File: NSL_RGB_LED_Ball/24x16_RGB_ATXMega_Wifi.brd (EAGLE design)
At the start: 46.4 x 123.7 mm, 109 parts, among them IC2 TLC5947XLP, IC3 TLC5947XLP, IC4 TLC5947XLP, IC5 MCP73123, IC6 BLUETOOTH-RN41", IC7 MMA7455L, IC8 OPA344, Q1 BSH201, X1 NX3225GA XC1972CT-ND

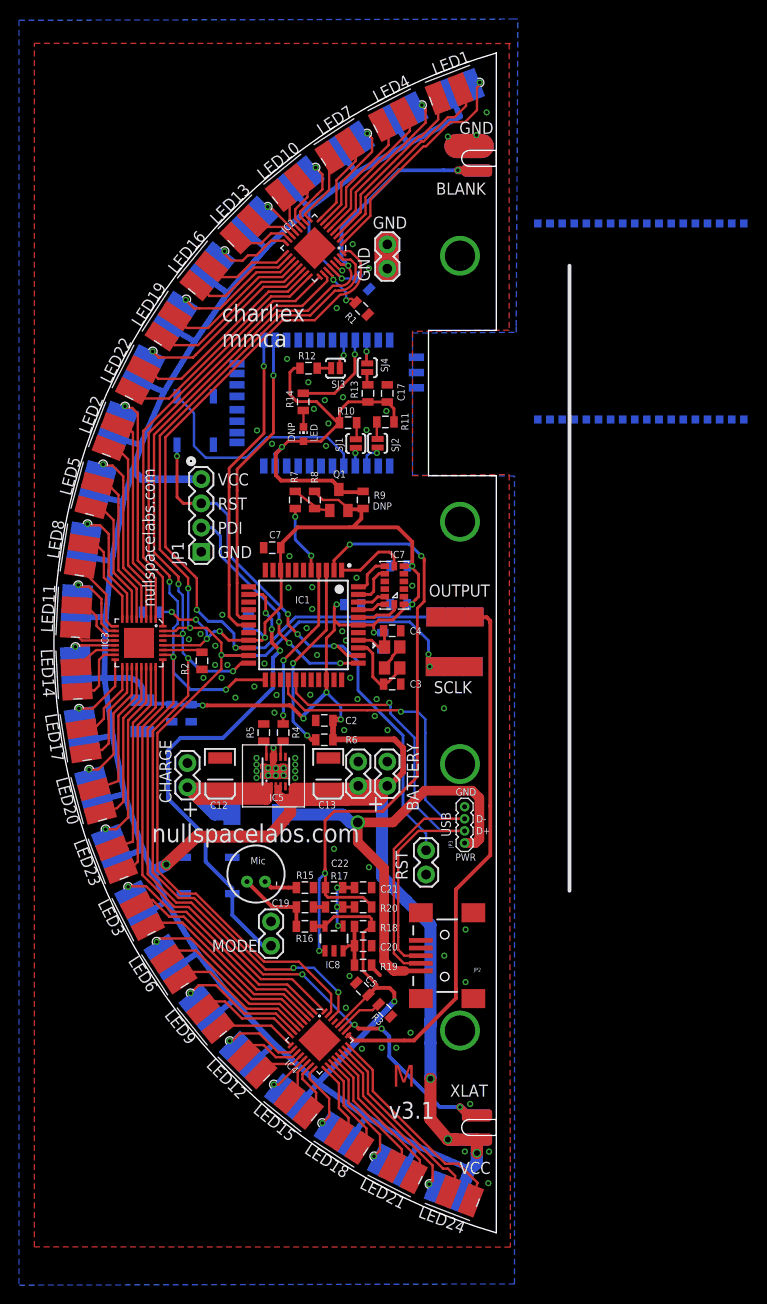
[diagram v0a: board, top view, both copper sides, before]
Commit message: 
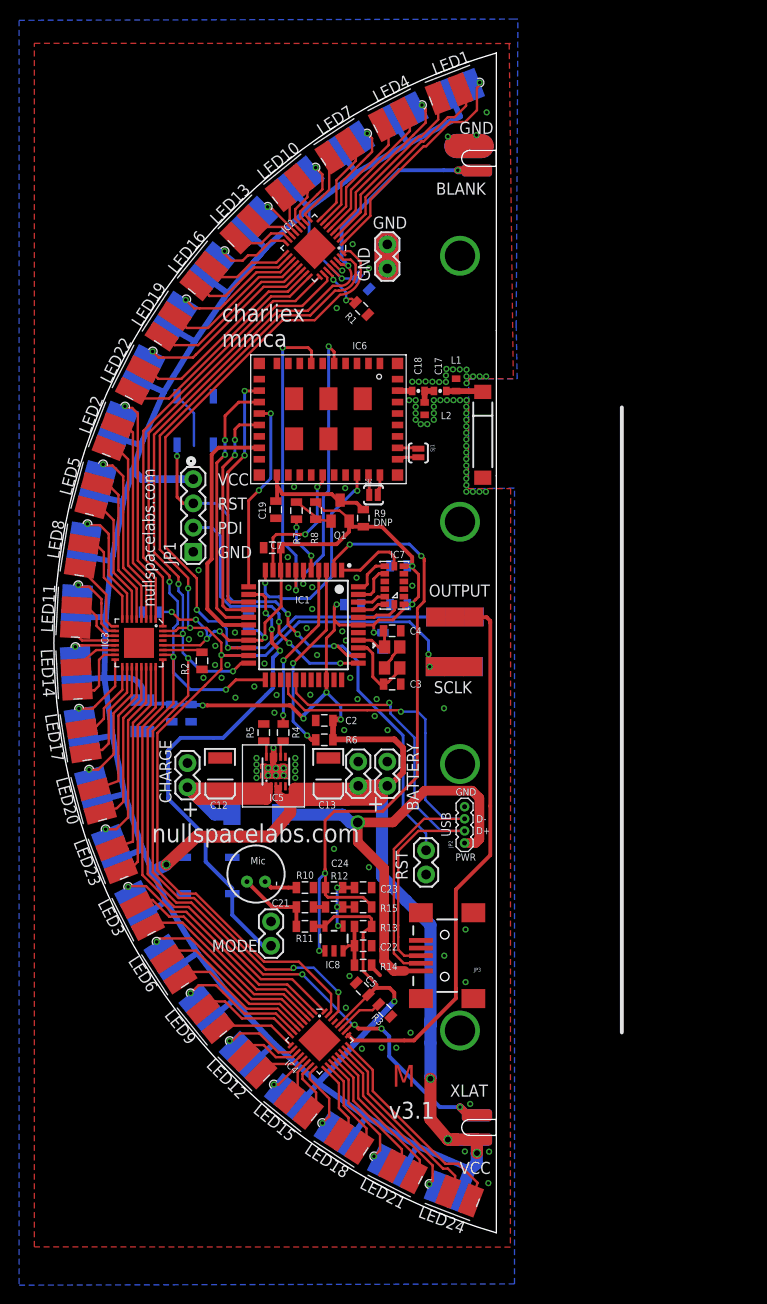
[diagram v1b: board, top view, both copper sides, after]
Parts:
- removed LED: (no value), led:CHIP-LED0603
- removed R16: 2.2k, SparkFun:0805
- removed R17, R18, R19: 10k, SparkFun:0805
- removed R20: 1M, SparkFun:0805
- removed SJ3, SJ4: SOLDERJUMPERNO, SparkFun:SJ_2S-NO
- removed U$5: ZG2100MC, zg2100-mrf24wb0ma:ZG2100MC
- added ANT: ANTENNA2SMD2, SparkFun:ANTENNA-CHIP3
- added C23: .1uF, SparkFun:0805
- added C24: 12pF, SparkFun:0805
- added L1: NL, SparkFun:C0402
- added L2: 2.2nH, SparkFun:C0402
- C17: value .1uF -> 2.2pF; device SparkFun:0805 -> SparkFun:0402-CAP
- C18: value 0.1uF -> 10pF; device SparkFun:0805 -> SparkFun:0402-CAP
- C19: value 4.7uF -> 1uF
- C20: value 1uF -> 0.1uF
- C21: value .1uF -> 4.7uF
- C22: value 12pF -> 1uF
- IC6: value BLUETOOTH-RN41" -> CC3000; device NSL_Mini_Quad:RN41 -> centerblack_engineering:CC3000
- JP2: value USBSMD -> (none); device SparkFun-Connectors:USB-MINIB -> SparkFun-Connectors:1X04-1.27MM
- JP3: value (none) -> USBSMD; device SparkFun-Connectors:1X04-1.27MM -> SparkFun-Connectors:USB-MINIB
- R10: value 1k -> 4.7k
- R11: value 1k -> 2.2k
- R12, R13: value 1k -> 10k
- R14: value 220 -> 10k
- R15: value 4.7k -> 1M
- moved R14 59.4 mm to (-31.8, -33.8), turned to 0 degrees
- moved R12 56.6 mm to (-34.8, -27.7)
- moved R13 55.9 mm to (-31.8, -29.7), turned to 0 degrees
- moved R11 53.6 mm to (-37.8, -29.7)
- moved R10 49.0 mm to (-37.8, -25.7)
- moved C19 41.8 mm to (-40.9, 14.0), turned to 90 degrees
- moved C20 40.0 mm to (-28.0, 8.08), flipped to the bottom
- moved C18 18.5 mm to (-26.0, 26.4), flipped to the top
- moved JP2 12.0 mm to (-21.1, -21.0), turned to 90 degrees
- moved JP3 12.0 mm to (-23.2, -32.8), turned to 180 degrees
- moved IC6 9.44 mm to (-43.5, 30.2), flipped to the top, turned to 270 degrees
- moved C22 6.82 mm to (-31.8, -31.8), turned to 180 degrees
- moved SJ1 6.63 mm to (-26.0, 19.9), turned to 270 degrees
- moved C21 6.43 mm to (-37.8, -27.7)
- moved R15 6.43 mm to (-31.8, -27.7), turned to 0 degrees
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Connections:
- removed net N$21: R12.1, SJ3.2
- removed net N$23: R11.1, SJ2.2
- removed net N$24: R13.1, SJ4.2
- removed net N$4: LED.C, R14.2
- removed net N$5: R10.1, SJ1.2
- removed net PIO3: IC6.20, SJ3.1
- removed net PIO4: IC6.22, SJ4.1
- removed net PIO5: IC6.21, R14.1
- removed net PIO6: IC6.3, SJ2.1
- removed net PIO7: IC6.4, SJ1.1
- removed net RX: IC1.16, IC6.14
- removed net TX: IC1.17, IC6.13
- new net MISO: IC1.16, IC6.P$13
- new net MOSI: IC1.15, IC6.P$15
- new net N$22: C17.2, C18.1, L2.2
- new net N$25: ANT.FEED, C17.1, L1.2
- new net N$26: IC6.P$30, SJ1.1
- new net N$27: IC6.P$29, SJ1.2
- new net N$28: IC6.P$28, SJ2.2
- new net N$29: IC6.P$27, SJ2.1
- new net N$8: C18.2, IC6.P$35
- new net SCK: IC1.17, IC6.P$17
- new net SPI_IRQ: IC1.12, IC6.P$14
- new net SS: IC1.14, IC6.P$12
- new net VBAT_SW_EN: IC1.11, IC6.P$26
- new net VIO: IC1.10, IC6.P$23
- new net WL_EN1: IC1.7, IC6.P$7
- new net WL_EN2: IC1.6, IC6.P$5
- net BT_RST: no longer IC6.5
- net D+: now also JP2.2, JP3.D+; no longer JP2.D+, JP3.2
- net D-: now also JP2.3, JP3.D-; no longer JP2.D-, JP3.3
- net GND: now also C19.1, C22.1, C23.2, IC6.P$1, IC6.P$10, IC6.P$11, IC6.P$16, IC6.P$18, IC6.P$20, IC6.P$21, IC6.P$22, IC6.P$25, IC6.P$31, IC6.P$32, IC6.P$33, IC6.P$34, IC6.P$36, IC6.P$37, IC6.P$38, IC6.P$39, IC6.P$40, IC6.P$41, IC6.P$42, IC6.P$43, IC6.P$44, IC6.P$45, IC6.P$46, IC6.P$9, JP2.4, JP3.GND, L1.1, L2.1, R10.1, R14.2; no longer C17.2, C18.1, C21.2, IC6.1, IC6.12, IC6.25, IC6.27, IC6.28, IC6.29, JP2.GND, JP3.4, R15.1, R19.2
- net MIC: now also C24.1, R15.2; no longer C22.1, R20.2
- net N$14: now also C21.2, R12.2; no longer C19.2, R17.2
- net N$15: now also C21.1, R11.1; no longer C19.1, R16.1
- net N$16: now also C22.2, R13.1, R14.1; no longer C20.2, R18.1, R19.1
- net N$17: now also C23.1, C24.2, R12.1, R15.1; no longer C21.1, C22.2, R17.1, R20.1
- net N$20: now also R10.2; no longer R15.2
- net N$7: now also JP2.1, JP3.VBUS; no longer JP2.VBUS, JP3.1
- net VCC: now also C20.2, R11.2, R13.2; no longer C18.2, R16.2, R18.2
- net VDD: now also C19.2, IC6.P$19; no longer C17.1, IC6.11, LED.A, R10.2, R11.2, R12.2, R13.2
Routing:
- net TX: track 33.0 -> 0.00 mm, vias 1 -> 0
- net WL_EN1: track 0.00 -> 32.6 mm, vias 0 -> 2
- net RX: track 31.8 -> 0.00 mm, vias 1 -> 0
- net WL_EN2: track 0.00 -> 29.5 mm, vias 0 -> 2
- net VDD: track 42.2 -> 13.4 mm, vias 1 -> 0
- net MISO: track 0.00 -> 28.5 mm, vias 0 -> 2
- net SCK: track 0.00 -> 26.7 mm
- net SS: track 0.00 -> 26.4 mm, vias 0 -> 2
- net MOSI: track 0.00 -> 24.7 mm, vias 0 -> 2
- net VBAT_SW_EN: track 0.00 -> 22.5 mm, vias 0 -> 2
- net SPI_IRQ: track 0.00 -> 20.3 mm, vias 0 -> 2
- net BT_RST: track 25.0 -> 5.94 mm
- net VIO: track 0.00 -> 13.9 mm, vias 0 -> 2
- net PIO5: track 9.86 -> 0.00 mm, vias 1 -> 0
- net VCC: track 543.6 -> 538.0 mm
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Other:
- outline, holes or cut-outs redrawn

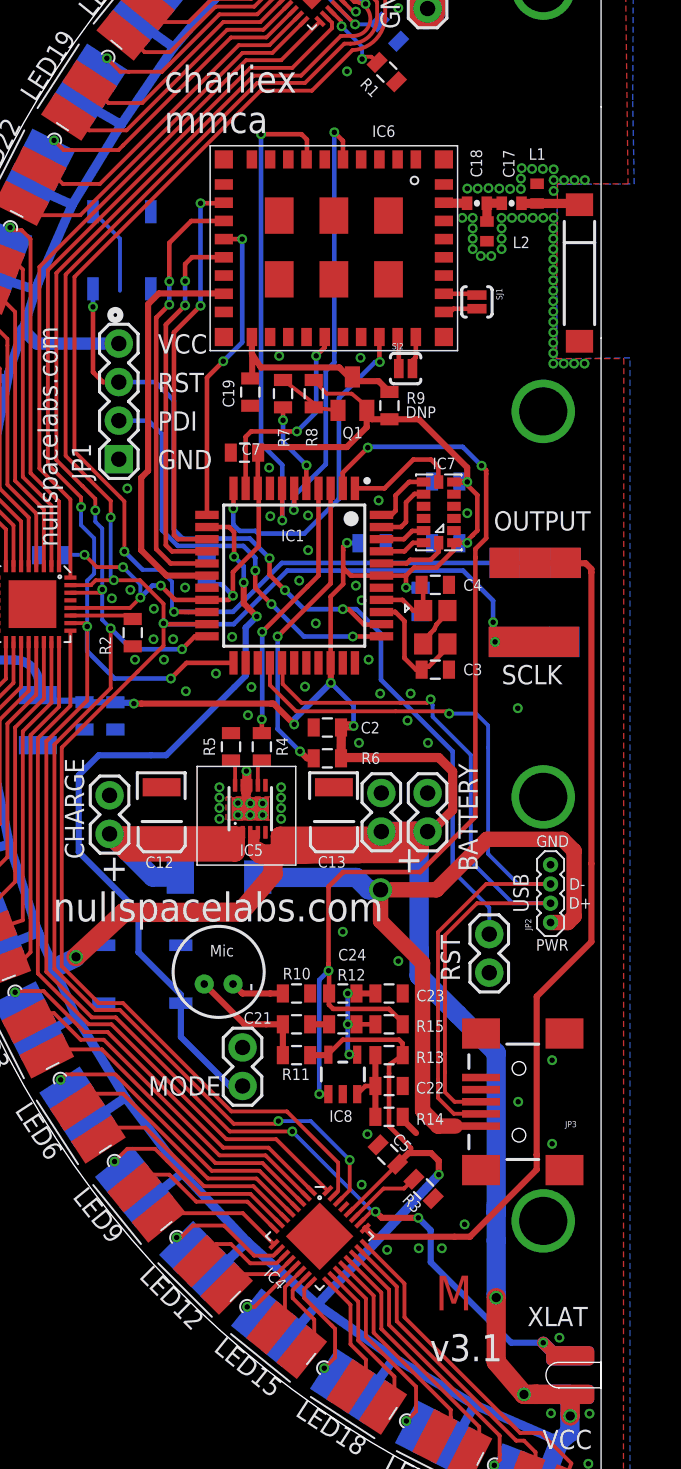
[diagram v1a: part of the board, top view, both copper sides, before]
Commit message: 
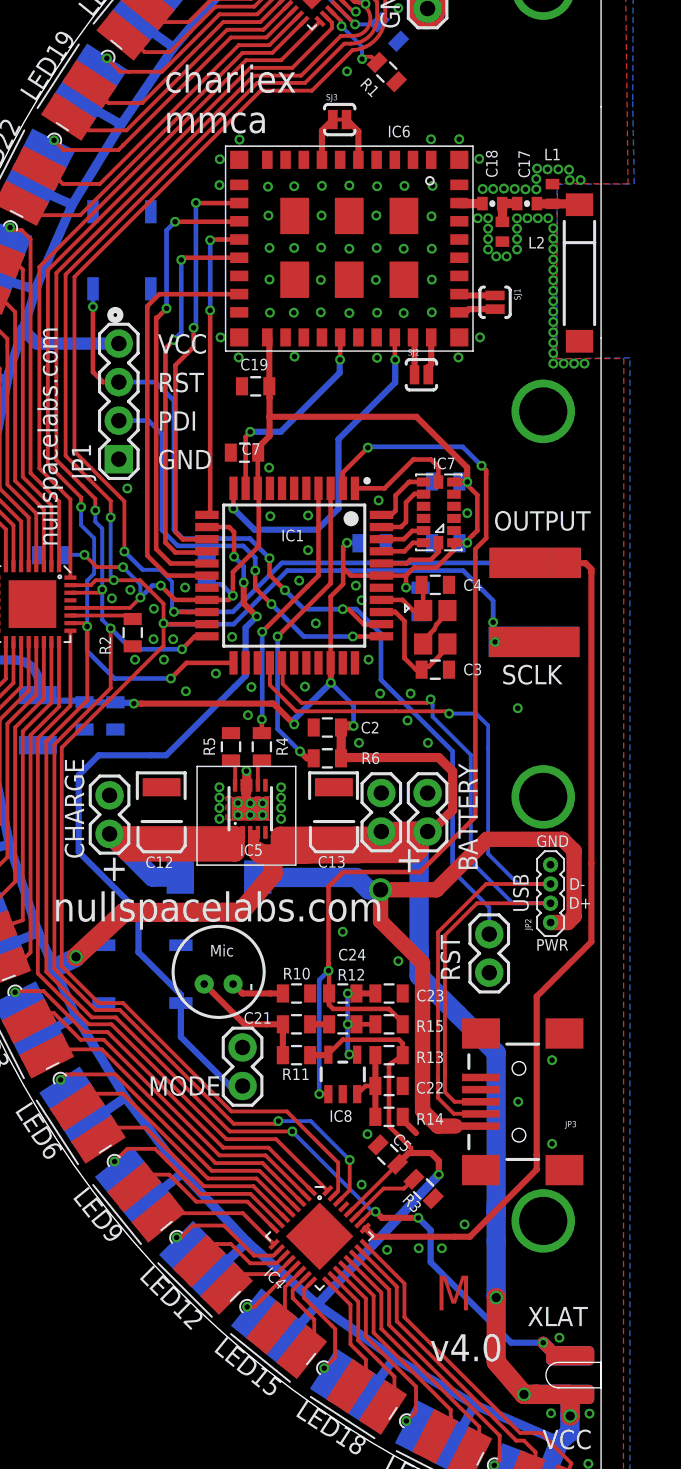
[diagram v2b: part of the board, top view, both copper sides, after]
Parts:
- removed Q1: BSH201, transistor-small-signal:SOT23
- removed R7, R8: 10k, SparkFun:0805
- removed R9: 0ohm DNP, SparkFun:0805
- added SJ3: SOLDERJUMPERNO, SparkFun:SJ_2S-NO
- moved SJ1 1.19 mm to (-24.8, 19.9)
- moved SJ2 1.12 mm to (-29.6, 15.1)
- moved IC6 1.02 mm to (-42.5, 30.2)
- moved C18 1.02 mm to (-24.9, 26.4)
- moved L2 1.02 mm to (-24.3, 24.5)
- moved L1 1.02 mm to (-21.0, 27.0)
- moved C17 1.02 mm to (-22.7, 26.4)
- moved C19 0.52 mm to (-40.5, 14.4), turned to 0 degrees
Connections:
- removed net BT_PWR: IC1.5, R7.2
- removed net N$18: Q1.1, R7.1, R8.1
- removed net VDD: C19.2, IC6.P$19, Q1.3, R9.1
- removed net WL_EN2: IC1.6, IC6.P$5
- net VCC: now also C19.2, IC6.P$19; no longer Q1.2, R8.2, R9.2
- net WL_EN1: now also IC6.P$5, SJ3.1, SJ3.2; no longer IC1.7
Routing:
- net WL_EN2: track 29.5 -> 0.00 mm, vias 2 -> 0
- net WL_EN1: track 32.6 -> 6.83 mm, vias 2 -> 0
- net VDD: track 13.4 -> 0.00 mm
- net BT_PWR: track 5.99 -> 0.00 mm, vias 2 -> 0
- net BT_RST: track 5.94 -> 0.00 mm
- net N$18: track 4.60 -> 0.00 mm
- net MISO: track 28.5 -> 30.1 mm
- net MOSI: track 24.7 -> 26.0 mm
- net SS: track 26.4 -> 27.4 mm
- net N$25: track 3.84 -> 3.16 mm
- net SCK: track 26.7 -> 27.3 mm
- net VCC: track 538.0 -> 538.5 mm
- net GND: vias 121 -> 155
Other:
- board text added: "v4.0"
- board text removed: "DNP"
- board text removed: "v3.1"
